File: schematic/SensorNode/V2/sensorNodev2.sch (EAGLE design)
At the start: 28 parts, among them IC1 V_REG_LD1117VXX, U1 ATMEGA328P_PDIP

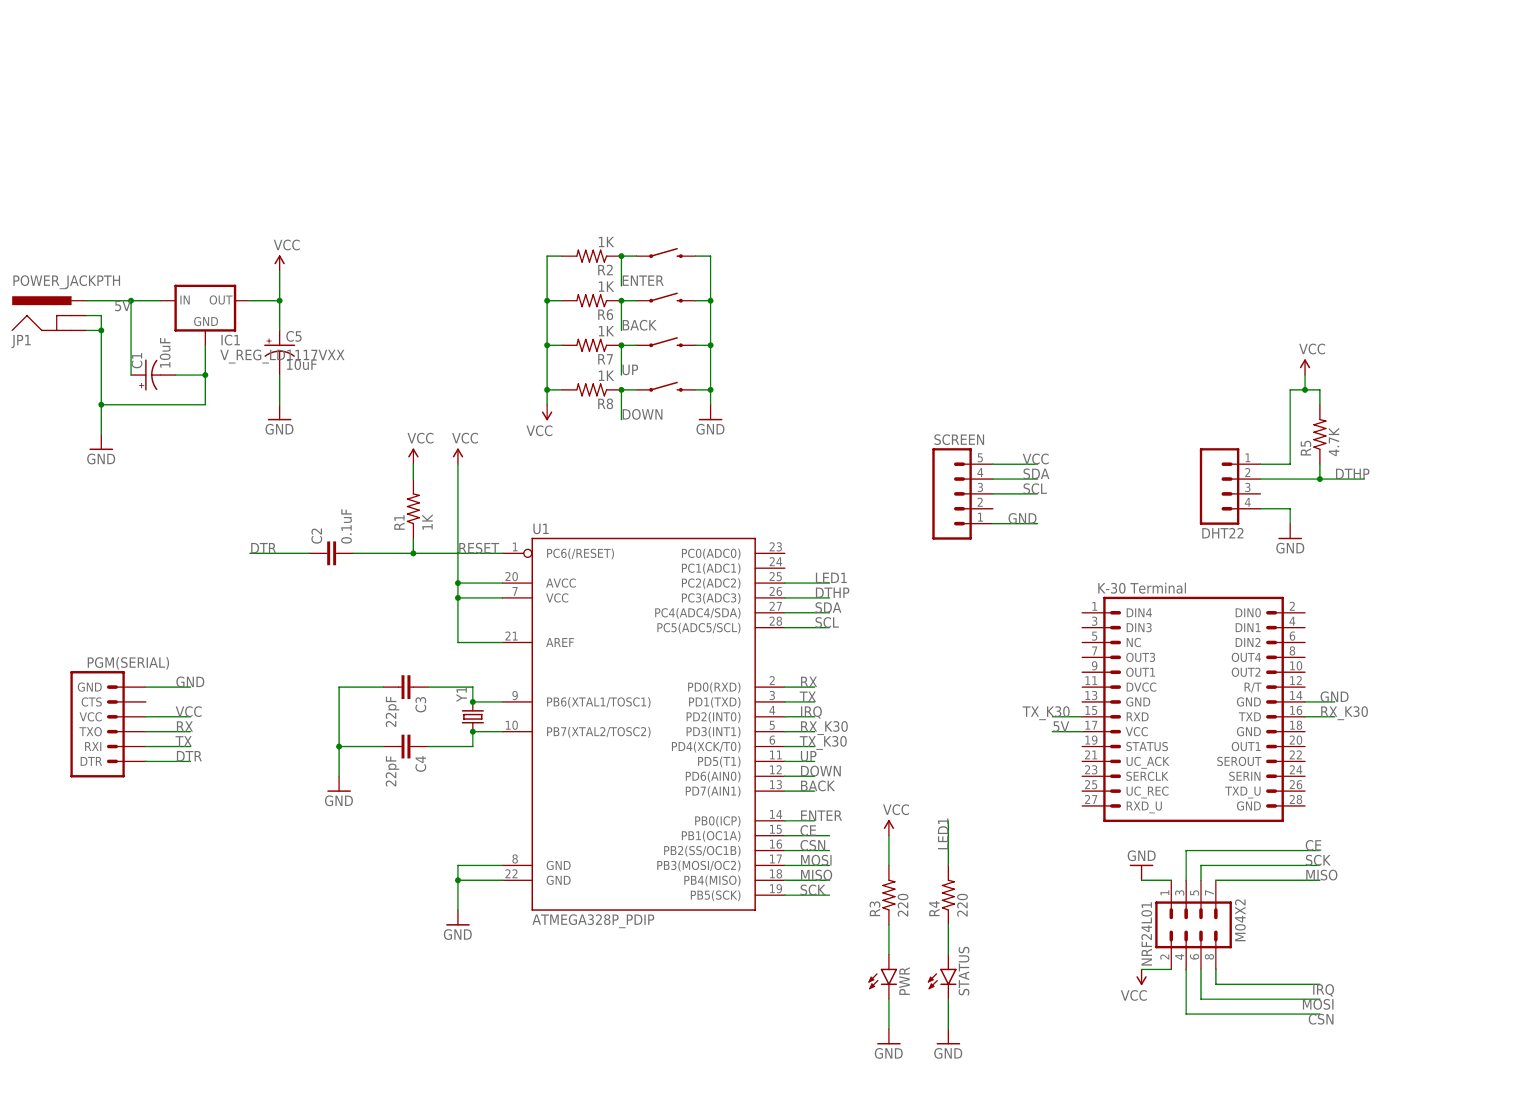
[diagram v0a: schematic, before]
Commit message: Updating sensor node and gateway node schematics
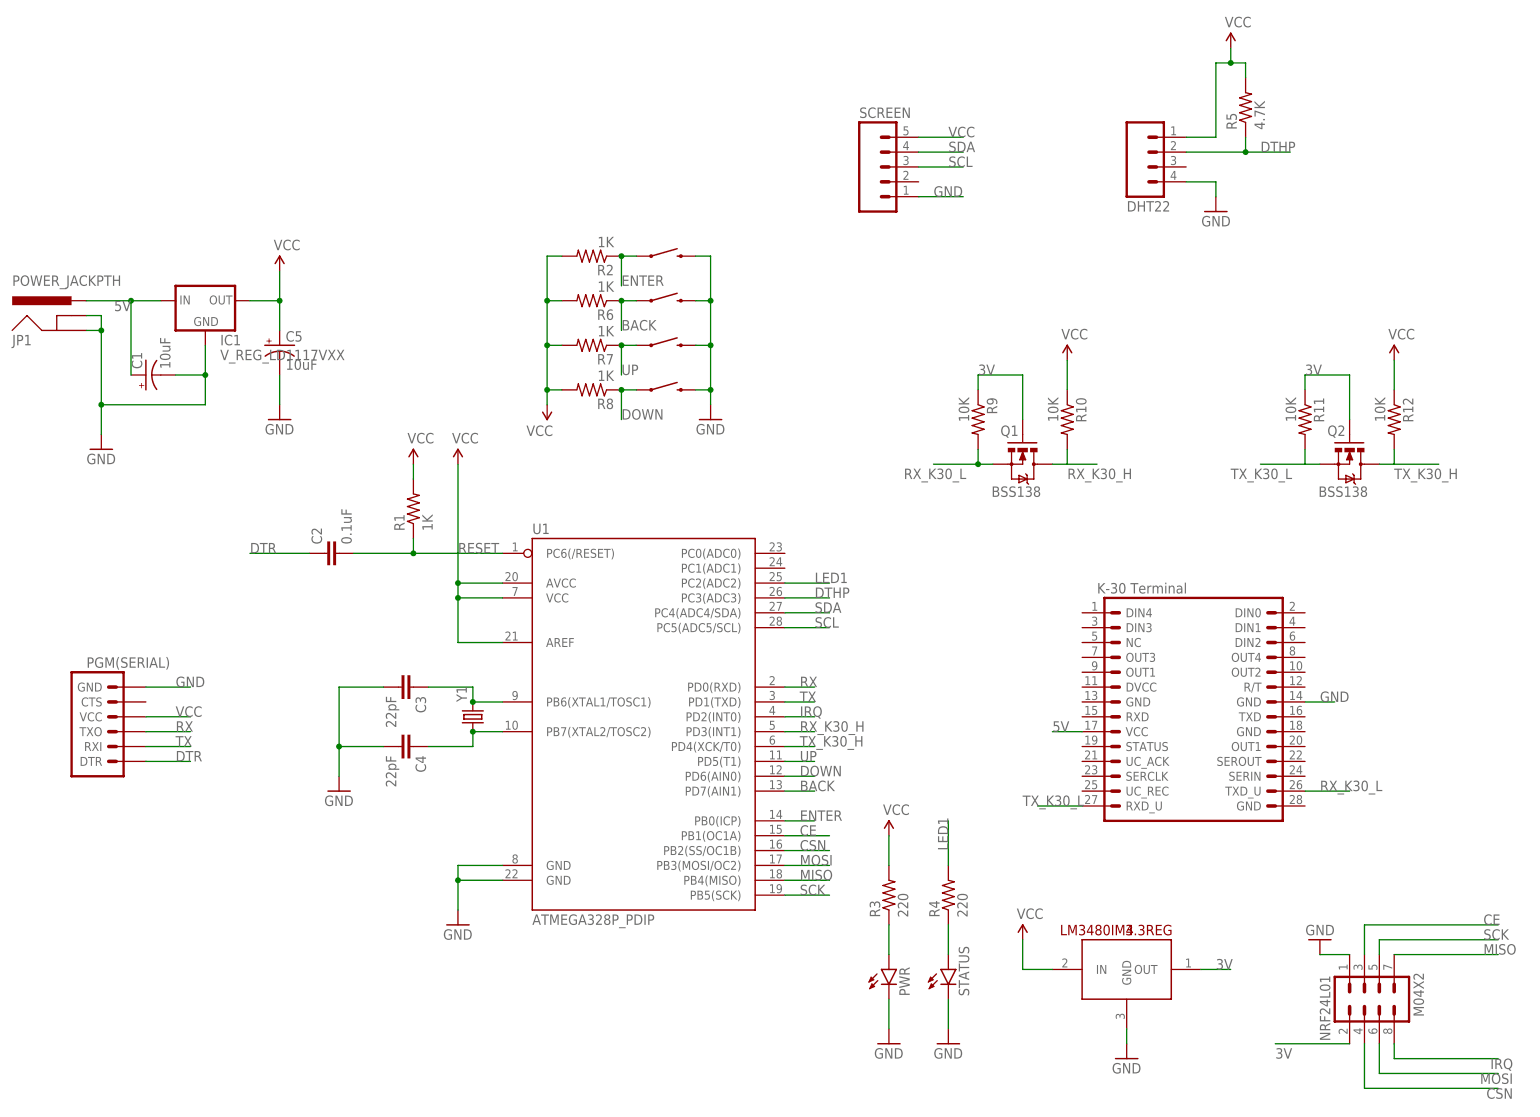
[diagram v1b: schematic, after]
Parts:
- added 3.3REG: LM3480IM4, SparkFun-PowerIC:LM3480IM4
- added Q1, Q2: BSS138, SparkFun:MOSFET-NCHANNELSMD
- added R10, R11, R12, R9: 10K, SparkFun:RESISTOR0603-RES
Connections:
- removed net RX_K30: JP3.TXD, U1.PD3(INT1)
- removed net TX_K30: JP3.RXD, U1.PD4(XCK/T0)
- new net 3V: 3.3REG.OUT, NRF24L01.2, Q1.G, Q2.G, R11.1, R9.1
- new net RX_K30_H: Q1.D, R10.2, U1.PD3(INT1)
- new net RX_K30_L: JP3.TXD_U, Q1.S, R9.2
- new net TX_K30_H: Q2.D, R12.2, U1.PD4(XCK/T0)
- new net TX_K30_L: JP3.RXD_U, Q2.S, R11.2
- net GND: now also 3.3REG.GND
- net VCC: now also 3.3REG.IN, R10.1, R12.1; no longer NRF24L01.2
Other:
- moved on the sheet: DHT22, NRF24L01, R5, SCREEN
